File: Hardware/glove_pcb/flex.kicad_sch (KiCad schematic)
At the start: 16 parts, among them J7 Potentiometers, J8 Potentiometers

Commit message: Finish changes according to feedback
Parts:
- added CR1, CR2, CR3, CR4: PESD4USB5B-TTSX, SOT1165D_NEX, symbol Glove_Symbols:PESD4USB5B-TTSX
- renumbered R20 to R16, R21 to R17, R22 to R18, R23 to R19, R24 to R20, R25 to R21, R26 to R22, R27 to R23, R28 to R24, R29 to R25, R30 to R26, R31 to R27, R32 to R28, R33 to R29
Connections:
- net GND: now also CR1.3 (GND), CR1.8 (GND), CR2.1 (CH1), CR2.3 (GND), CR2.8 (GND), CR3.3 (GND), CR3.8 (GND), CR4.3 (GND), CR4.5 (CH4), CR4.8 (GND)
- net POT_INDEX_1: now also CR1.2 (CH2)
- net POT_INDEX_2: now also CR1.1 (CH1)
- net POT_INDEX_3: now also CR2.5 (CH4)
- net POT_MIDDLE_1: now also CR2.4 (CH3)
- net POT_MIDDLE_2: now also CR2.2 (CH2)
- net POT_MIDDLE_3: now also CR4.4 (CH3)
- net POT_PINKY_1: now also CR3.4 (CH3)
- net POT_PINKY_2: now also CR3.2 (CH2)
- net POT_PINKY_3: now also CR3.1 (CH1)
- net POT_RING_1: now also CR4.2 (CH2)
- net POT_RING_2: now also CR3.5 (CH4), CR4.1 (CH1)
- net POT_THUMB_1: now also CR1.5 (CH4)
- net POT_THUMB_2: now also CR1.4 (CH3)
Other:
- moved on the sheet: J8, R23, R24, R25, R26, R27, R28, R29

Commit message: Finish schematic updates
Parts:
- removed CR1, CR2, CR3, CR4: PESD4USB5B-TTSX, SOT1165D_NEX, symbol Glove_Symbols:PESD4USB5B-TTSX
- added U10, U11, U8, U9: BZA408B, SOT457_NXP, symbol Glove_Symbols:BZA408B
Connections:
- net GND: now also U10.2 (GND), U10.5 (GND), U11.2 (GND), U11.5 (GND), U11.6 (K4), U8.2 (GND), U8.5 (GND), U9.2 (GND), U9.5 (GND), U9.6 (K4)
- net POT_INDEX_2: now also U8.6 (K4)
- net POT_INDEX_3: now also U8.4 (K3), U9.1 (K1)
- net POT_MIDDLE_1: now also U9.3 (K2)
- net POT_MIDDLE_2: now also U9.4 (K3)
- net POT_MIDDLE_3: now also U11.4 (K3)
- net POT_PINKY_1: now also U10.4 (K3)
- net POT_PINKY_2: now also U10.3 (K2)
- net POT_PINKY_3: now also U10.1 (K1)
- net POT_RING_1: now also U11.3 (K2)
- net POT_RING_2: now also U11.1 (K1)
- net POT_RING_3: now also U10.6 (K4)
- net POT_THUMB_1: now also U8.1 (K1)
- net POT_THUMB_2: now also U8.3 (K2)

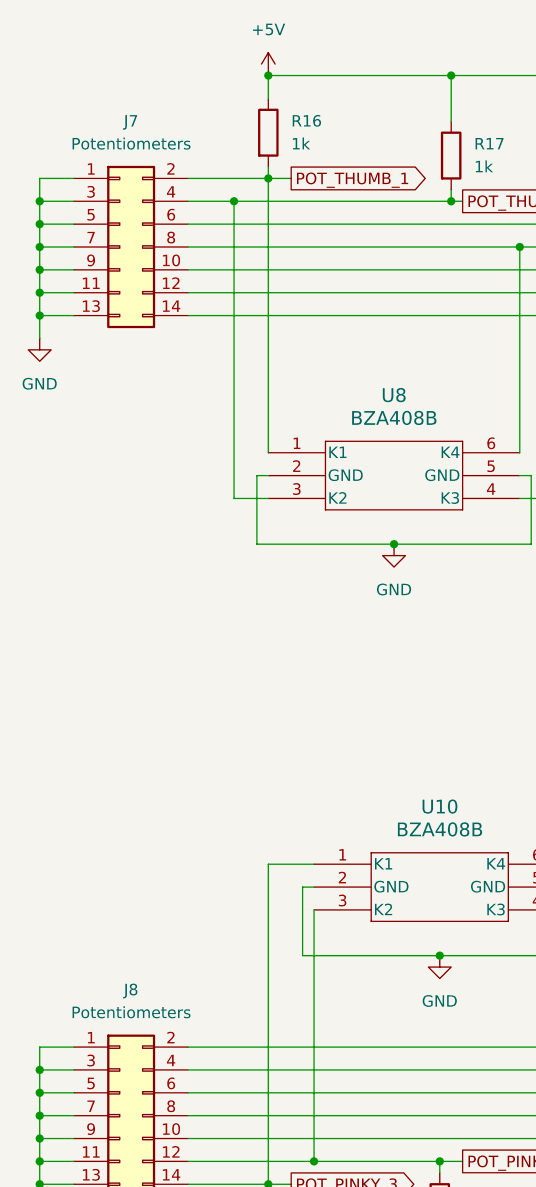
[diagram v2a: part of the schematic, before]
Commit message: More updates to the schematic based on Dmitry's feedback
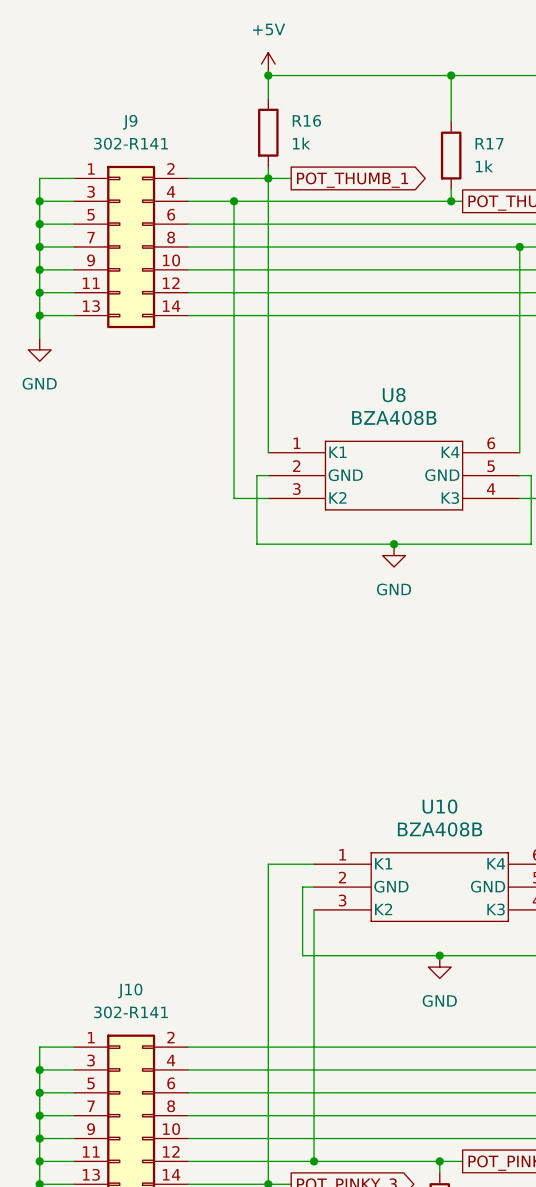
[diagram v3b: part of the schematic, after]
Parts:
- J10: renamed from J8; value Potentiometers -> 302-R141
- J9: renamed from J7; value Potentiometers -> 302-R141
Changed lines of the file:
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@@
   (title_block
     (title "Flex Potentiometer Connections")
-    (date "2023-11-24")
+    (date "2024-01-24")
     (company "COEN 490 Team 15")
   )
@@
   (symbol (lib_id "Connector_Generic:Conn_02x07_Odd_Even") (at 41.91 39.37 0) (unit 1)
     (in_bom yes) (on_board yes) (dnp no) (fields_autoplaced)
-    (property "Reference" "J7" (at 43.18 25.4 0)
+    (property "Reference" "J9" (at 43.18 25.4 0)
       (effects (font (size 1.27 1.27)))
     )
-    (property "Value" "Potentiometers" (at 43.18 27.94 0)
+    (property "Value" "302-R141" (at 43.18 27.94 0)
       (effects (font (size 1.27 1.27)))
     )
@@
       (project "glove_pcb"
         (path "/747ff5f3-d342-40b0-8e4e-75b3a3063e75/bbbc9975-a050-48bd-8c18-11f2eff17087"
-          (reference "J7") (unit 1)
+          (reference "J9") (unit 1)
         )
       )
@@
   (symbol (lib_id "Connector_Generic:Conn_02x07_Odd_Even") (at 41.91 135.89 0) (unit 1)
     (in_bom yes) (on_board yes) (dnp no) (fields_autoplaced)
-    (property "Reference" "J8" (at 43.18 121.92 0)
+    (property "Reference" "J10" (at 43.18 121.92 0)
       (effects (font (size 1.27 1.27)))
     )
-    (property "Value" "Potentiometers" (at 43.18 124.46 0)
+    (property "Value" "302-R141" (at 43.18 124.46 0)
       (effects (font (size 1.27 1.27)))
     )
@@
       (project "glove_pcb"
         (path "/747ff5f3-d342-40b0-8e4e-75b3a3063e75/bbbc9975-a050-48bd-8c18-11f2eff17087"
-          (reference "J8") (unit 1)
-        )
-      )
+          (reference "J10") (unit 1)
+        )
+      )

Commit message: Change isp pin symbol
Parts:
- U10, U11, U8, U9: footprint SOT457_NXP -> Glove_Footprints:SOT457_NXP
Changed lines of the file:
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@@
       (effects (font (size 1.524 1.524)))
     )
-    (property "Footprint" "SOT457_NXP" (at 62.23 107.95 0)
+    (property "Footprint" "Glove_Footprints:SOT457_NXP" (at 62.23 107.95 0)
       (effects (font (size 1.27 1.27) italic) hide)
     )
@@
       (effects (font (size 1.524 1.524)))
     )
-    (property "Footprint" "SOT457_NXP" (at 132.08 62.23 0)
+    (property "Footprint" "Glove_Footprints:SOT457_NXP" (at 132.08 62.23 0)
       (effects (font (size 1.27 1.27) italic) hide)
     )
@@
       (effects (font (size 1.524 1.524)))
     )
-    (property "Footprint" "SOT457_NXP" (at 57.15 62.23 0)
+    (property "Footprint" "Glove_Footprints:SOT457_NXP" (at 57.15 62.23 0)
       (effects (font (size 1.27 1.27) italic) hide)
     )
@@
       (effects (font (size 1.524 1.524)))
     )
-    (property "Footprint" "SOT457_NXP" (at 132.08 107.95 0)
-      (effects (font (size 1.27 1.27) italic) hide)
-    )
+    (property "Footprint" "Glove_Footprints:SOT457_NXP" (at 132.08 107.95 0)
+      (effects (font (size 1.27 1.27) italic) hide)
+    )

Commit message: Changes before & during meeting
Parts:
- J10, J9: footprint Connector_PinSocket_2.54mm:PinSocket_2x07_P2.54mm_Vertical -> Connector_PinSocket_2.54mm:PinSocket_2x07_P2.54mm_Horizontal
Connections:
- net GND: now also J10.10 (Pin_10), J10.12 (Pin_12), J10.14 (Pin_14), J10.2 (Pin_2), J10.4 (Pin_4), J10.6 (Pin_6), J10.8 (Pin_8), J9.10 (Pin_10), J9.12 (Pin_12), J9.14 (Pin_14), J9.2 (Pin_2), J9.4 (Pin_4), J9.6 (Pin_6), J9.8 (Pin_8); no longer J10.1 (Pin_1), J10.11 (Pin_11), J10.13 (Pin_13), J10.3 (Pin_3), J10.5 (Pin_5), J10.7 (Pin_7), J10.9 (Pin_9), J9.1 (Pin_1), J9.11 (Pin_11), J9.13 (Pin_13), J9.3 (Pin_3), J9.5 (Pin_5), J9.7 (Pin_7), J9.9 (Pin_9)
- net POT_INDEX_1: now also J9.5 (Pin_5); no longer J9.6 (Pin_6)
- net POT_INDEX_2: now also J9.7 (Pin_7); no longer J9.8 (Pin_8)
- net POT_INDEX_3: now also J9.9 (Pin_9); no longer J9.10 (Pin_10)
- net POT_MIDDLE_1: now also J9.11 (Pin_11); no longer J9.12 (Pin_12)
- net POT_MIDDLE_2: now also J9.13 (Pin_13); no longer J9.14 (Pin_14)
- net POT_MIDDLE_3: now also J10.1 (Pin_1); no longer J10.2 (Pin_2)
- net POT_PINKY_1: now also J10.9 (Pin_9); no longer J10.10 (Pin_10)
- net POT_PINKY_2: now also J10.11 (Pin_11); no longer J10.12 (Pin_12)
- net POT_PINKY_3: now also J10.13 (Pin_13); no longer J10.14 (Pin_14)
- net POT_RING_1: now also J10.3 (Pin_3); no longer J10.4 (Pin_4)
- net POT_RING_2: now also J10.5 (Pin_5); no longer J10.6 (Pin_6)
- net POT_RING_3: now also J10.7 (Pin_7); no longer J10.8 (Pin_8)
- net POT_THUMB_1: now also J9.1 (Pin_1); no longer J9.2 (Pin_2)
- net POT_THUMB_2: now also J9.3 (Pin_3); no longer J9.4 (Pin_4)
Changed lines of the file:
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@@
   (junction (at 151.13 20.32) (diameter 0) (color 0 0 0 0)
   )
-  (wire (pts (xy 36.83 44.45) (xy 33.02 44.45))
-    (stroke (width 0) (type default))
-  )
   (wire (pts (xy 97.79 36.83) (xy 99.06 36.83))
     (stroke (width 0) (type default))
@@
     (stroke (width 0) (type default))
   )
-  (wire (pts (xy 36.83 135.89) (xy 33.02 135.89))
-    (stroke (width 0) (type default))
-  )
   (wire (pts (xy 162.56 62.23) (xy 162.56 64.77))
     (stroke (width 0) (type default))
@@
     (stroke (width 0) (type default))
   )
+  (wire (pts (xy 33.02 36.83) (xy 36.83 36.83))
+    (stroke (width 0) (type default))
+  )
   (wire (pts (xy 86.36 64.77) (xy 87.63 64.77))
     (stroke (width 0) (type default))
@@
     (stroke (width 0) (type default))
   )
+  (wire (pts (xy 33.02 143.51) (xy 36.83 143.51))
+    (stroke (width 0) (type default))
+  )
   (wire (pts (xy 78.74 34.29) (xy 80.01 34.29))
     (stroke (width 0) (type default))
@@
     (stroke (width 0) (type default))
   )
+  (wire (pts (xy 33.02 133.35) (xy 36.83 133.35))
+    (stroke (width 0) (type default))
+  )
   (wire (pts (xy 33.02 34.29) (xy 33.02 36.83))
     (stroke (width 0) (type default))
   )
-  (wire (pts (xy 36.83 130.81) (xy 33.02 130.81))
-    (stroke (width 0) (type default))
-  )
   (wire (pts (xy 114.3 144.78) (xy 114.3 154.94))
     (stroke (width 0) (type default))
@@
     (stroke (width 0) (type default))
   )
-  (wire (pts (xy 36.83 143.51) (xy 33.02 143.51))
+  (wire (pts (xy 33.02 39.37) (xy 36.83 39.37))
     (stroke (width 0) (type default))
   )
@@
     (stroke (width 0) (type default))
   )
+  (wire (pts (xy 33.02 41.91) (xy 36.83 41.91))
+    (stroke (width 0) (type default))
+  )
   (wire (pts (xy 49.53 138.43) (xy 91.44 138.43))
     (stroke (width 0) (type default))
@@
     (stroke (width 0) (type default))
   )
-  (wire (pts (xy 36.83 46.99) (xy 33.02 46.99))
-    (stroke (width 0) (type default))
-  )
   (wire (pts (xy 115.57 38.1) (xy 115.57 39.37))
     (stroke (width 0) (type default))
@@
     (stroke (width 0) (type default))
   )
-  (wire (pts (xy 36.83 39.37) (xy 33.02 39.37))
-    (stroke (width 0) (type default))
-  )
   (wire (pts (xy 162.56 107.95) (xy 162.56 110.49))
     (stroke (width 0) (type default))
@@
     (stroke (width 0) (type default))
   )
+  (wire (pts (xy 33.02 140.97) (xy 36.83 140.97))
+    (stroke (width 0) (type default))
+  )
+  (wire (pts (xy 33.02 130.81) (xy 36.83 130.81))
+    (stroke (width 0) (type default))
+  )
   (wire (pts (xy 162.56 110.49) (xy 162.56 118.11))
     (stroke (width 0) (type default))
@@
     (stroke (width 0) (type default))
   )
-  (wire (pts (xy 36.83 34.29) (xy 33.02 34.29))
+  (wire (pts (xy 33.02 138.43) (xy 36.83 138.43))
+    (stroke (width 0) (type default))
+  )
+  (wire (pts (xy 33.02 34.29) (xy 36.83 34.29))
     (stroke (width 0) (type default))
   )
@@
     (stroke (width 0) (type default))
   )
-  (wire (pts (xy 36.83 140.97) (xy 33.02 140.97))
-    (stroke (width 0) (type default))
-  )
   (wire (pts (xy 58.42 67.31) (xy 54.61 67.31))
     (stroke (width 0) (type default))
@@
     (stroke (width 0) (type default))
   )
-  (wire (pts (xy 36.83 128.27) (xy 33.02 128.27))
+  (wire (pts (xy 33.02 128.27) (xy 36.83 128.27))
     (stroke (width 0) (type default))
   )
@@
     (stroke (width 0) (type default))
   )
-  (wire (pts (xy 36.83 41.91) (xy 33.02 41.91))
-    (stroke (width 0) (type default))
-  )
   (wire (pts (xy 33.02 31.75) (xy 33.02 34.29))
     (stroke (width 0) (type default))
@@
     (stroke (width 0) (type default))
   )
-  (wire (pts (xy 36.83 138.43) (xy 33.02 138.43))
-    (stroke (width 0) (type default))
-  )
   (wire (pts (xy 115.57 39.37) (xy 116.84 39.37))
     (stroke (width 0) (type default))
@@
     (stroke (width 0) (type default))
   )
+  (wire (pts (xy 33.02 46.99) (xy 36.83 46.99))
+    (stroke (width 0) (type default))
+  )
   (wire (pts (xy 77.47 140.97) (xy 80.01 140.97))
     (stroke (width 0) (type default))
@@
     (stroke (width 0) (type default))
   )
+  (wire (pts (xy 33.02 135.89) (xy 36.83 135.89))
+    (stroke (width 0) (type default))
+  )
   (wire (pts (xy 133.35 64.77) (xy 132.08 64.77))
     (stroke (width 0) (type default))
@@
     (stroke (width 0) (type default))
   )
+  (wire (pts (xy 33.02 44.45) (xy 36.83 44.45))
+    (stroke (width 0) (type default))
+  )
   (wire (pts (xy 166.37 46.99) (xy 170.18 46.99))
     (stroke (width 0) (type default))
@@
     (stroke (width 0) (type default))
   )
-  (wire (pts (xy 36.83 36.83) (xy 33.02 36.83))
-    (stroke (width 0) (type default))
-  )
   (wire (pts (xy 151.13 20.32) (xy 170.18 20.32))
     (stroke (width 0) (type default))
@@
     (stroke (width 0) (type default))
   )
-  (wire (pts (xy 36.83 133.35) (xy 33.02 133.35))
-    (stroke (width 0) (type default))
-  )
   (wire (pts (xy 58.42 143.51) (xy 60.96 143.51))
     (stroke (width 0) (type default))
   )
-  (wire (pts (xy 36.83 31.75) (xy 33.02 31.75))
+  (wire (pts (xy 33.02 31.75) (xy 36.83 31.75))
     (stroke (width 0) (type default))
   )
@@
     )
   )
-  (symbol (lib_id "Connector_Generic:Conn_02x07_Odd_Even") (at 41.91 39.37 0) (unit 1)
-    (in_bom yes) (on_board yes) (dnp no) (fields_autoplaced)
+  (symbol (lib_id "Connector_Generic:Conn_02x07_Odd_Even") (at 44.45 39.37 0) (mirror y) (unit 1)
+    (in_bom yes) (on_board yes) (dnp no)
     (property "Reference" "J9" (at 43.18 25.4 0)
       (effects (font (size 1.27 1.27)))
@@
       (effects (font (size 1.27 1.27)))
     )
-    (property "Footprint" "Connector_PinSocket_2.54mm:PinSocket_2x07_P2.54mm_Vertical" (at 41.91 39.37 0)
-      (effects (font (size 1.27 1.27)) hide)
-    )
-    (property "Datasheet" "~" (at 41.91 39.37 0)
+    (property "Footprint" "Connector_PinSocket_2.54mm:PinSocket_2x07_P2.54mm_Horizontal" (at 44.45 39.37 0)
+      (effects (font (size 1.27 1.27)) hide)
+    )
+    (property "Datasheet" "~" (at 44.45 39.37 0)
       (effects (font (size 1.27 1.27)) hide)
     )
@@
     )
   )
-  (symbol (lib_id "Connector_Generic:Conn_02x07_Odd_Even") (at 41.91 135.89 0) (unit 1)
-    (in_bom yes) (on_board yes) (dnp no) (fields_autoplaced)
+  (symbol (lib_id "Connector_Generic:Conn_02x07_Odd_Even") (at 44.45 135.89 0) (mirror y) (unit 1)
+    (in_bom yes) (on_board yes) (dnp no)
     (property "Reference" "J10" (at 43.18 121.92 0)
       (effects (font (size 1.27 1.27)))
@@
       (effects (font (size 1.27 1.27)))
     )
-    (property "Footprint" "Connector_PinSocket_2.54mm:PinSocket_2x07_P2.54mm_Vertical" (at 41.91 135.89 0)
-      (effects (font (size 1.27 1.27)) hide)
-    )
-    (property "Datasheet" "~" (at 41.91 135.89 0)
-      (effects (font (size 1.27 1.27)) hide)
-    )
+    (property "Footprint" "Connector_PinSocket_2.54mm:PinSocket_2x07_P2.54mm_Horizontal" (at 44.45 135.89 0)
+      (effects (font (size 1.27 1.27)) hide)
+    )
+    (property "Datasheet" "~" (at 44.45 135.89 0)
+      (effects (font (size 1.27 1.27)) hide)
+    )

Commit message: Reworking placing
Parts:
- renumbered J9 to J5, J10 to J6
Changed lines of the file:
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@@
   (symbol (lib_id "Connector_Generic:Conn_02x07_Odd_Even") (at 44.45 39.37 0) (mirror y) (unit 1)
     (in_bom yes) (on_board yes) (dnp no)
-    (property "Reference" "J9" (at 43.18 25.4 0)
+    (property "Reference" "J5" (at 43.18 25.4 0)
       (effects (font (size 1.27 1.27)))
     )
@@
       (project "glove_pcb"
         (path "/747ff5f3-d342-40b0-8e4e-75b3a3063e75/bbbc9975-a050-48bd-8c18-11f2eff17087"
-          (reference "J9") (unit 1)
+          (reference "J5") (unit 1)
         )
       )
@@
   (symbol (lib_id "Connector_Generic:Conn_02x07_Odd_Even") (at 44.45 135.89 0) (mirror y) (unit 1)
     (in_bom yes) (on_board yes) (dnp no)
-    (property "Reference" "J10" (at 43.18 121.92 0)
+    (property "Reference" "J6" (at 43.18 121.92 0)
       (effects (font (size 1.27 1.27)))
     )
@@
       (project "glove_pcb"
         (path "/747ff5f3-d342-40b0-8e4e-75b3a3063e75/bbbc9975-a050-48bd-8c18-11f2eff17087"
-          (reference "J10") (unit 1)
-        )
-      )
+          (reference "J6") (unit 1)
+        )
+      )

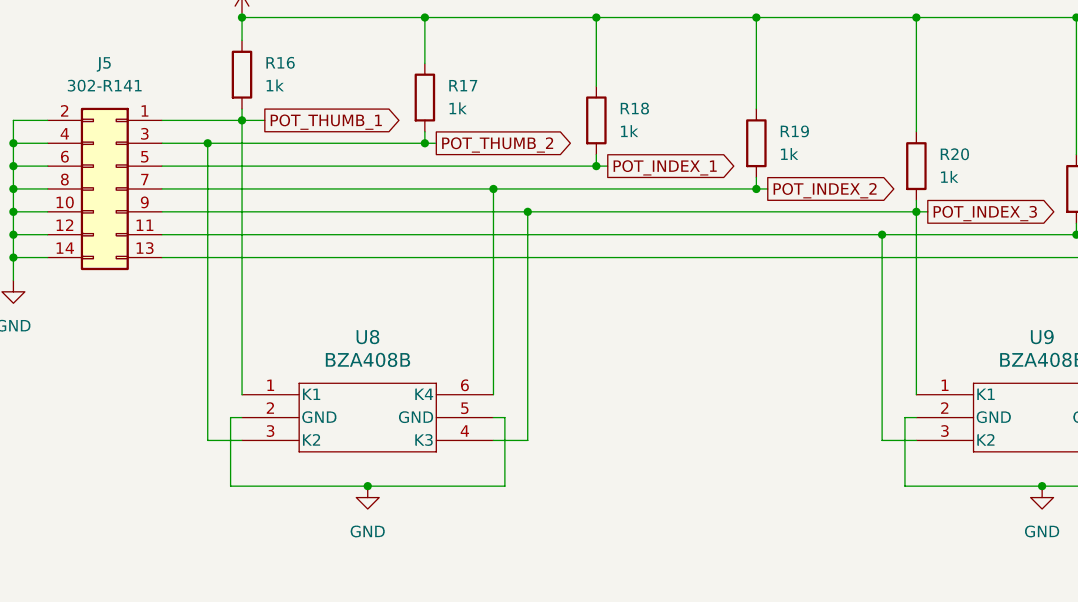
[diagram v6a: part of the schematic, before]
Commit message: Finish re-placing + draw copper zones
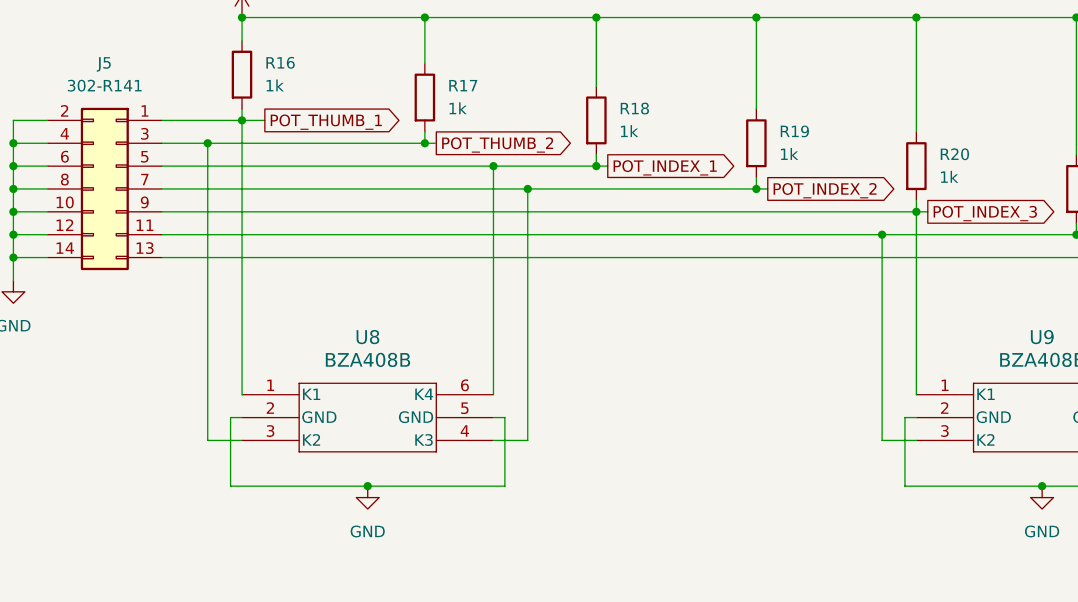
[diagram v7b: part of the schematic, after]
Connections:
- net POT_INDEX_1: now also U8.6 (K4)
- net POT_INDEX_2: now also U8.4 (K3); no longer U8.6 (K4)
- net POT_INDEX_3: no longer U8.4 (K3)
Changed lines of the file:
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@@
   (junction (at 58.42 20.32) (diameter 0) (color 0 0 0 0)
   )
-  (junction (at 90.17 41.91) (diameter 0) (color 0 0 0 0)
-  )
   (junction (at 78.74 20.32) (diameter 0) (color 0 0 0 0)
   )
+  (junction (at 86.36 36.83) (diameter 0) (color 0 0 0 0)
+  )
   (junction (at 63.5 140.97) (diameter 0) (color 0 0 0 0)
   )
@@
   (junction (at 114.3 135.89) (diameter 0) (color 0 0 0 0)
   )
+  (junction (at 90.17 39.37) (diameter 0) (color 0 0 0 0)
+  )
   (junction (at 33.02 39.37) (diameter 0) (color 0 0 0 0)
   )
@@
   (junction (at 133.35 41.91) (diameter 0) (color 0 0 0 0)
   )
-  (junction (at 86.36 39.37) (diameter 0) (color 0 0 0 0)
-  )
   (junction (at 147.32 154.94) (diameter 0) (color 0 0 0 0)
   )
@@
     (stroke (width 0) (type default))
   )
+  (wire (pts (xy 90.17 39.37) (xy 90.17 67.31))
+    (stroke (width 0) (type default))
+  )
   (wire (pts (xy 77.47 149.86) (xy 77.47 154.94))
     (stroke (width 0) (type default))
@@
     (stroke (width 0) (type default))
   )
+  (wire (pts (xy 86.36 36.83) (xy 97.79 36.83))
+    (stroke (width 0) (type default))
+  )
   (wire (pts (xy 86.36 64.77) (xy 87.63 64.77))
     (stroke (width 0) (type default))
@@
     (stroke (width 0) (type default))
   )
-  (wire (pts (xy 49.53 36.83) (xy 97.79 36.83))
+  (wire (pts (xy 49.53 36.83) (xy 86.36 36.83))
     (stroke (width 0) (type default))
   )
@@
     (stroke (width 0) (type default))
   )
+  (wire (pts (xy 90.17 39.37) (xy 115.57 39.37))
+    (stroke (width 0) (type default))
+  )
   (wire (pts (xy 162.56 107.95) (xy 162.56 110.49))
     (stroke (width 0) (type default))
@@
     (stroke (width 0) (type default))
   )
-  (wire (pts (xy 49.53 41.91) (xy 90.17 41.91))
+  (wire (pts (xy 49.53 41.91) (xy 133.35 41.91))
     (stroke (width 0) (type default))
   )
@@
     (stroke (width 0) (type default))
   )
-  (wire (pts (xy 86.36 39.37) (xy 86.36 62.23))
-    (stroke (width 0) (type default))
-  )
   (wire (pts (xy 96.52 135.89) (xy 114.3 135.89))
     (stroke (width 0) (type default))
@@
     (stroke (width 0) (type default))
   )
-  (wire (pts (xy 90.17 67.31) (xy 90.17 41.91))
-    (stroke (width 0) (type default))
-  )
-  (wire (pts (xy 49.53 39.37) (xy 86.36 39.37))
-    (stroke (width 0) (type default))
-  )
   (wire (pts (xy 87.63 64.77) (xy 87.63 72.39))
     (stroke (width 0) (type default))
@@
     (stroke (width 0) (type default))
   )
-  (wire (pts (xy 86.36 39.37) (xy 115.57 39.37))
+  (wire (pts (xy 49.53 39.37) (xy 90.17 39.37))
     (stroke (width 0) (type default))
   )
@@
     (stroke (width 0) (type default))
   )
-  (wire (pts (xy 90.17 41.91) (xy 133.35 41.91))
-    (stroke (width 0) (type default))
-  )
   (wire (pts (xy 162.56 64.77) (xy 162.56 72.39))
     (stroke (width 0) (type default))
@@
     (stroke (width 0) (type default))
   )
+  (wire (pts (xy 86.36 36.83) (xy 86.36 62.23))
+    (stroke (width 0) (type default))
+  )
